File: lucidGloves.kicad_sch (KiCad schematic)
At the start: 29 parts, among them J1 USB_C_Receptacle, J10 Conn_01x05_Pin, J11 Conn_01x05_Pin, J12 Conn_01x19_Socket, J13 Conn_01x05_Pin, J14 Conn_01x03_Pin, J15 Conn_01x03_Pin, J16 Conn_01x03_Pin, J17 Conn_01x03_Pin, J18 Conn_01x03_Pin, J2 USB_C_Receptacle, J3 Conn_01x05_Pin, J4 Conn_01x05_Pin, J5 Conn_01x05_Pin, J6 Conn_01x16_Pin, J7 Conn_01x08_Pin, J8 Conn_01x19_Socket, J9 Conn_01x05_Pin, SW2 SW_Push

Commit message: Correct PCB alignment and spacing
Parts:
- removed H1, H2, H4: MountingHole, MountingHole:MountingHole_3.2mm_M3, symbol Mechanical:MountingHole
- J13, J5: footprint Connector_PinHeader_2.54mm:PinHeader_1x05_P2.54mm_Vertical -> Connector_PinHeader_2.54mm:PinHeader_1x05_P2.54mm_Horizontal
- renumbered R7 to R1, R1 to R2, R5 to R3, SW2 to SW1
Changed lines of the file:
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@@
-	(symbol
-		(lib_id "Mechanical:MountingHole")
-		(at 41.91 74.93 0)
-		(unit 1)
-		(exclude_from_sim yes)
-		(in_bom no)
-		(on_board yes)
-		(dnp no)
-		(fields_autoplaced yes)
-		(property "Reference" "H4"
-			(at 44.45 73.6599 0)
-			(effects
-				(font
-					(size 1.27 1.27)
-				)
-				(justify left)
-			)
-		)
-		(property "Value" "MountingHole"
-			(at 44.45 76.1999 0)
-			(effects
-				(font
-					(size 1.27 1.27)
-				)
-				(justify left)
-			)
-		)
-		(property "Footprint" "MountingHole:MountingHole_3.2mm_M3"
-			(at 41.91 74.93 0)
-			(effects
-				(font
-					(size 1.27 1.27)
-				)
-				(hide yes)
-			)
-		)
-		(property "Datasheet" "~"
-			(at 41.91 74.93 0)
-			(effects
-				(font
-					(size 1.27 1.27)
-				)
-				(hide yes)
-			)
-		)
-		(property "Description" "Mounting Hole without connection"
-			(at 41.91 74.93 0)
-			(effects
-				(font
-					(size 1.27 1.27)
-				)
-				(hide yes)
-			)
-		)
-		(instances
-			(project "lucidGloves"
-				(path "/4ef451b9-c6da-41b6-b847-894b88f6d21b"
-					(reference "H4")
-					(unit 1)
-				)
-			)
-		)
-	)
 	(symbol
 		(lib_id "Mechanical:MountingHole")
@@
 		(on_board yes)
 		(dnp no)
-		(property "Reference" "R5"
+		(property "Reference" "R3"
 			(at 138.43 146.05 90)
 			(effects
@@
 			(project ""
 				(path "/4ef451b9-c6da-41b6-b847-894b88f6d21b"
-					(reference "R5")
+					(reference "R3")
 					(unit 1)
 				)
@@
 			)
 		)
-		(property "Footprint" "Connector_PinHeader_2.54mm:PinHeader_1x05_P2.54mm_Vertical"
+		(property "Footprint" "Connector_PinHeader_2.54mm:PinHeader_1x05_P2.54mm_Horizontal"
 			(at 228.6 114.3 0)
 			(effects
@@
 		(dnp no)
 		(fields_autoplaced yes)
-		(property "Reference" "SW2"
+		(property "Reference" "SW1"
 			(at 210.82 91.44 0)
 			(effects
@@
 			(project ""
 				(path "/4ef451b9-c6da-41b6-b847-894b88f6d21b"
-					(reference "SW2")
+					(reference "SW1")
 					(unit 1)
 				)
@@
 			)
 		)
-		(property "Footprint" "Connector_PinHeader_2.54mm:PinHeader_1x05_P2.54mm_Vertical"
+		(property "Footprint" "Connector_PinHeader_2.54mm:PinHeader_1x05_P2.54mm_Horizontal"
 			(at 121.92 116.84 0)
 			(effects
@@
 	)
 	(symbol
-		(lib_id "Mechanical:MountingHole")
-		(at 41.91 55.88 0)
-		(unit 1)
-		(exclude_from_sim yes)
-		(in_bom no)
-		(on_board yes)
-		(dnp no)
-		(fields_autoplaced yes)
-		(property "Reference" "H1"
-			(at 44.45 54.6099 0)
-			(effects
-				(font
-					(size 1.27 1.27)
-				)
-				(justify left)
-			)
-		)
-		(property "Value" "MountingHole"
-			(at 44.45 57.1499 0)
-			(effects
-				(font
-					(size 1.27 1.27)
-				)
-				(justify left)
-			)
-		)
-		(property "Footprint" "MountingHole:MountingHole_3.2mm_M3"
-			(at 41.91 55.88 0)
-			(effects
-				(font
-					(size 1.27 1.27)
-				)
-				(hide yes)
-			)
-		)
-		(property "Datasheet" "~"
-			(at 41.91 55.88 0)
-			(effects
-				(font
-					(size 1.27 1.27)
-				)
-				(hide yes)
-			)
-		)
-		(property "Description" "Mounting Hole without connection"
-			(at 41.91 55.88 0)
-			(effects
-				(font
-					(size 1.27 1.27)
-				)
-				(hide yes)
-			)
-		)
-		(instances
-			(project ""
-				(path "/4ef451b9-c6da-41b6-b847-894b88f6d21b"
-					(reference "H1")
-					(unit 1)
-				)
-			)
-		)
-	)
-	(symbol
 		(lib_id "Connector:Conn_01x16_Pin")
 		(at 142.24 81.28 90)
@@
 		(on_board yes)
 		(dnp no)
-		(property "Reference" "R1"
+		(property "Reference" "R2"
 			(at 88.9 130.81 90)
 			(effects
@@
 			(project "lucidGloves"
 				(path "/4ef451b9-c6da-41b6-b847-894b88f6d21b"
-					(reference "R1")
+					(reference "R2")
 					(unit 1)
 				)
@@
 		(on_board yes)
 		(dnp no)
-		(property "Reference" "R7"
+		(property "Reference" "R1"
 			(at 48.26 130.81 90)
 			(effects
@@
 			(project "lucidGloves"
 				(path "/4ef451b9-c6da-41b6-b847-894b88f6d21b"
-					(reference "R7")
+					(reference "R1")
 					(unit 1)
 				)
@@
 					(unit 1)
 				)
-			)
-		)
-	)
-	(symbol
-		(lib_id "Mechanical:MountingHole")
-		(at 41.91 62.23 0)
-		(unit 1)
-		(exclude_from_sim yes)
-		(in_bom no)
-		(on_board yes)
-		(dnp no)
-		(fields_autoplaced yes)
-		(property "Reference" "H2"
-			(at 44.45 60.9599 0)
-			(effects
-				(font
-					(size 1.27 1.27)
-				)
-				(justify left)
-			)
-		)
-		(property "Value" "MountingHole"
-			(at 44.45 63.4999 0)
-			(effects
-				(font
-					(size 1.27 1.27)
-				)
-				(justify left)
-			)
-		)
-		(property "Footprint" "MountingHole:MountingHole_3.2mm_M3"
-			(at 41.91 62.23 0)
-			(effects
-				(font
-					(size 1.27 1.27)
-				)
-				(hide yes)
-			)
-		)
-		(property "Datasheet" "~"
-			(at 41.91 62.23 0)
-			(effects
-				(font
-					(size 1.27 1.27)
-				)
-				(hide yes)
-			)
-		)
-		(property "Description" "Mounting Hole without connection"
-			(at 41.91 62.23 0)
-			(effects
-				(font
-					(size 1.27 1.27)
-				)
-				(hide yes)
-			)
-		)
-		(instances
-			(project "lucidGloves"
-				(path "/4ef451b9-c6da-41b6-b847-894b88f6d21b"
-					(reference "H2")
-					(unit 1)
-				)

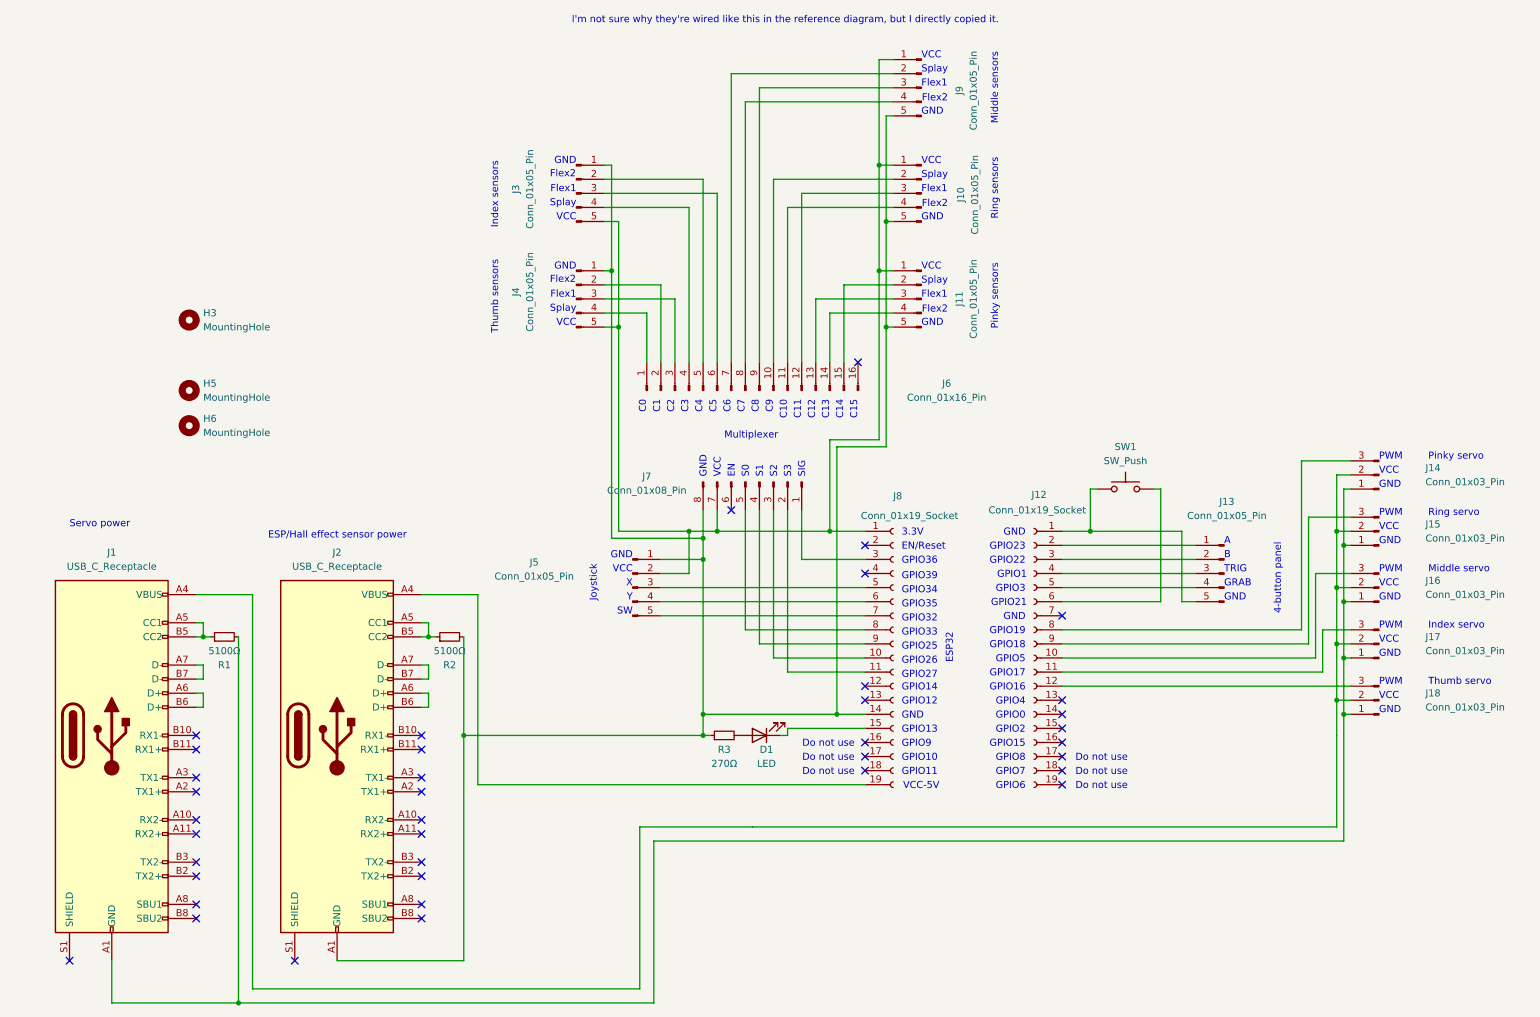
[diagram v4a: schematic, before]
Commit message: Start routing wires and change USB C ports again
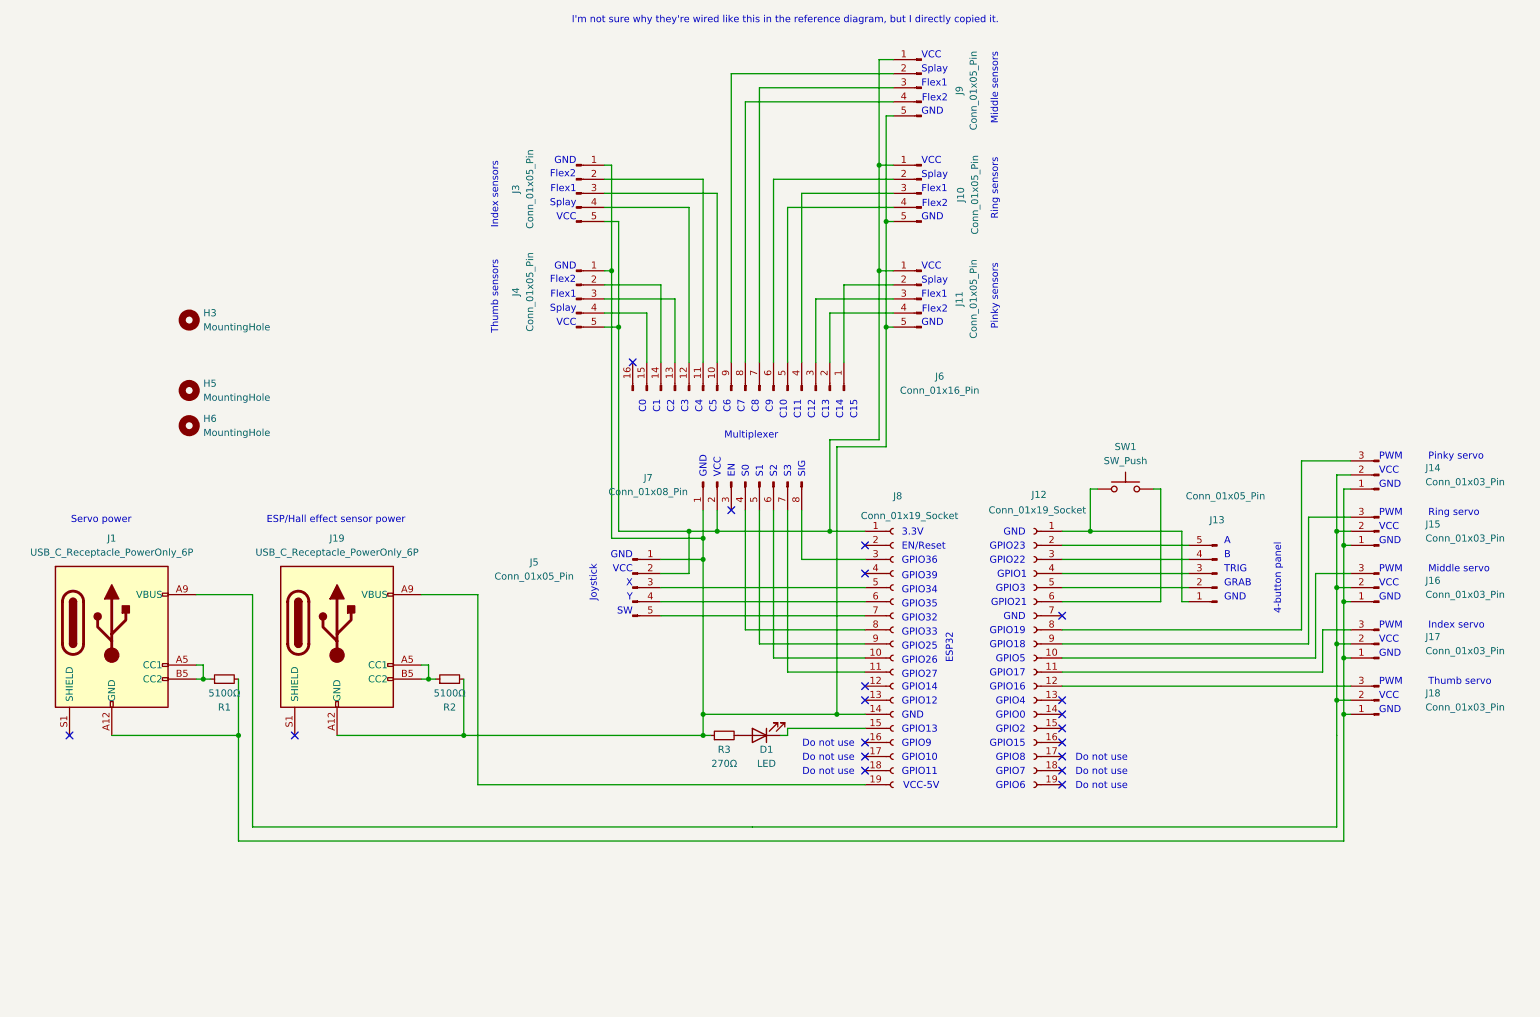
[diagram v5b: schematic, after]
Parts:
- removed J1, J2: USB_C_Receptacle, Connector_USB:USB_C_Receptacle_Molex_105450-0101, symbol Connector:USB_C_Receptacle
- added J1, J19: USB_C_Receptacle_PowerOnly_6P, symbol Connector:USB_C_Receptacle_PowerOnly_6P
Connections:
- net at J12.1 (Pin_1), SW1.1: now also J13.1 (Pin_1); no longer J13.5 (Pin_5)
- net at J12.2 (Pin_2): now also J13.5 (Pin_5); no longer J13.1 (Pin_1)
- net at J12.3 (Pin_3): now also J13.4 (Pin_4); no longer J13.2 (Pin_2)
- net at J12.5 (Pin_5): now also J13.2 (Pin_2); no longer J13.4 (Pin_4)
- net at J14.1 (Pin_1), J15.1 (Pin_1), J16.1 (Pin_1)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: now also J1.A12 (GND), J1.B12 (GND)
- net at J14.2 (Pin_2), J15.2 (Pin_2), J16.2 (Pin_2)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: now also J1.A9 (VBUS), J1.B9 (VBUS)
- net at R1.1: now also J1.A5 (CC1), J1.B5 (CC2)
- net at J10.1 (Pin_1), J11.1 (Pin_1), J3.5 (Pin_5)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: now also J7.2 (Pin_2); no longer J7.7 (Pin_7)
- net at J11.2 (Pin_2): now also J6.1 (Pin_1); no longer J6.15 (Pin_15)
- net at J11.3 (Pin_3): now also J6.3 (Pin_3); no longer J6.13 (Pin_13)
- net at J11.4 (Pin_4): now also J6.2 (Pin_2); no longer J6.14 (Pin_14)
- net at J10.5 (Pin_5), J11.5 (Pin_5), J3.1 (Pin_1)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: now also J7.1 (Pin_1), J19.A12 (GND), J19.B12 (GND); no longer J7.8 (Pin_8)
- net at J8.19 (Pin_19): now also J19.A9 (VBUS), J19.B9 (VBUS)
- net at R2.1: now also J19.A5 (CC1), J19.B5 (CC2)
- net at J4.2 (Pin_2): now also J6.14 (Pin_14); no longer J6.2 (Pin_2)
- net at J4.3 (Pin_3): now also J6.13 (Pin_13); no longer J6.3 (Pin_3)
- net at J4.4 (Pin_4): now also J6.15 (Pin_15); no longer J6.1 (Pin_1)
- net at J3.2 (Pin_2): now also J6.11 (Pin_11); no longer J6.5 (Pin_5)
- net at J3.3 (Pin_3): now also J6.10 (Pin_10); no longer J6.6 (Pin_6)
- net at J3.4 (Pin_4): now also J6.12 (Pin_12); no longer J6.4 (Pin_4)
- net at J10.2 (Pin_2): now also J6.6 (Pin_6); no longer J6.10 (Pin_10)
- net at J10.3 (Pin_3): now also J6.4 (Pin_4); no longer J6.12 (Pin_12)
- net at J10.4 (Pin_4): now also J6.5 (Pin_5); no longer J6.11 (Pin_11)
- net at J8.3 (Pin_3): now also J7.8 (Pin_8); no longer J7.1 (Pin_1)
- net at J8.11 (Pin_11): now also J7.7 (Pin_7); no longer J7.2 (Pin_2)
- net at J7.3 (Pin_3): no longer J8.10 (Pin_10)
- net at J7.4 (Pin_4): now also J8.8 (Pin_8); no longer J8.9 (Pin_9)
- net at J7.5 (Pin_5): now also J8.9 (Pin_9); no longer J8.8 (Pin_8)
- net at J7.6 (Pin_6): now also J8.10 (Pin_10)
- net at J6.7 (Pin_7): now also J9.3 (Pin_3); no longer J9.2 (Pin_2)
- net at J6.9 (Pin_9): now also J9.2 (Pin_2); no longer J9.3 (Pin_3)
- no-connect marks 39 -> 19
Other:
- moved on the sheet: J13, J6, J7, R1, R2

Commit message: Finish PCB
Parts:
- J1, J19: footprint (none) -> Connector_USB:USB_C_Receptacle_GCT_USB4135-GF-A_6P_TopMnt_Horizontal
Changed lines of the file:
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@@
 			)
 		)
-		(property "Footprint" ""
+		(property "Footprint" "Connector_USB:USB_C_Receptacle_GCT_USB4135-GF-A_6P_TopMnt_Horizontal"
 			(at 72.39 123.19 0)
 			(effects
@@
 			)
 		)
-		(property "Footprint" ""
+		(property "Footprint" "Connector_USB:USB_C_Receptacle_GCT_USB4135-GF-A_6P_TopMnt_Horizontal"
 			(at 31.75 123.19 0)
 			(effects

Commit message: Many improvements and tweaks
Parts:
- added H2: MountingHole, MountingHole:MountingHole_3.2mm_M3, symbol Mechanical:MountingHole
- added J14: Conn_01x06_Pin, Connector_PinHeader_2.54mm:PinHeader_1x06_P2.54mm_Horizontal, symbol Connector:Conn_01x06_Pin
- added J3: Conn_01x03_Pin, Connector_PinHeader_2.54mm:PinHeader_1x03_P2.54mm_Horizontal, symbol Connector:Conn_01x03_Pin
- D1: footprint LED_THT:LED_D5.0mm -> LED_SMD:LED_PLCC-2_3.4x3.0mm_AK
- renumbered H3 to H1, H5 to H3, H6 to H4, J9 to J10, J10 to J11, J11 to J12, J12 to J13, J13 to J15, J14 to J16, J15 to J17, J16 to J18, J17 to J19, J19 to J2, J18 to J20, J3 to J4, J4 to J5, J5 to J6, J6 to J7, J7 to J8, J8 to J9
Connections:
- net at J13.13 (Pin_13): now also J14.6 (Pin_6)
- net at J13.14 (Pin_14): now also J14.5 (Pin_5)
- net at J13.15 (Pin_15): now also J14.4 (Pin_4)
- net at J13.16 (Pin_16): now also J14.3 (Pin_3)
- net at J10.1 (Pin_1), J11.1 (Pin_1), J12.1 (Pin_1)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: now also J3.1 (Pin_1)
- net at J10.5 (Pin_5), J11.5 (Pin_5), J12.5 (Pin_5)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: now also J3.2 (Pin_2)
- net at J2.A9 (VBUS), J2.B9 (VBUS), J9.19 (Pin_19): now also J3.3 (Pin_3)
- net at J9.12 (Pin_12): now also J14.1 (Pin_1)
- net at J9.13 (Pin_13): now also J14.2 (Pin_2)
- no-connect marks 19 -> 13

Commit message: Tweaks for final JLCPCB order
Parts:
- D1: footprint LED_SMD:LED_PLCC-2_3.4x3.0mm_AK -> LED_SMD:LED_PLCC-2_3x2mm_AK; LCSC (none) -> C2286
- H1, H2, H3, H4: LCSC (none) -> -
- J1, J2: LCSC (none) -> C2681548
- J10, J11, J12, J4, J5: LCSC (none) -> C5156614
- J13, J9: LCSC (none) -> C319202
- J14: LCSC (none) -> C56816
- J15, J6: LCSC (none) -> C138801
- J16, J17, J18, J19, J20: LCSC (none) -> C49257
- J3: LCSC (none) -> C92159
- J7: LCSC (none) -> C7501270
- J8: LCSC (none) -> C5156616
- R1, R2: footprint Resistor_SMD:R_0603_1608Metric -> Resistor_SMD:R_0402_1005Metric; LCSC (none) -> C103079
- R3: footprint Resistor_SMD:R_0603_1608Metric -> Resistor_SMD:R_0402_1005Metric; LCSC (none) -> C138294
- SW1: LCSC (none) -> C271750
